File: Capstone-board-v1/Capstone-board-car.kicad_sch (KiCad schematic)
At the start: 25 parts, among them J1 Pcio Socket 1, J2 Pico Socket 2, J3 Ultra Sonic Sensor, J4 Car, J5 Camera, U1 3.3V Voltage Regulator, U2 555 Timer, U3 5V Voltage Regulator 2, U4 5V Voltage Regulator 1

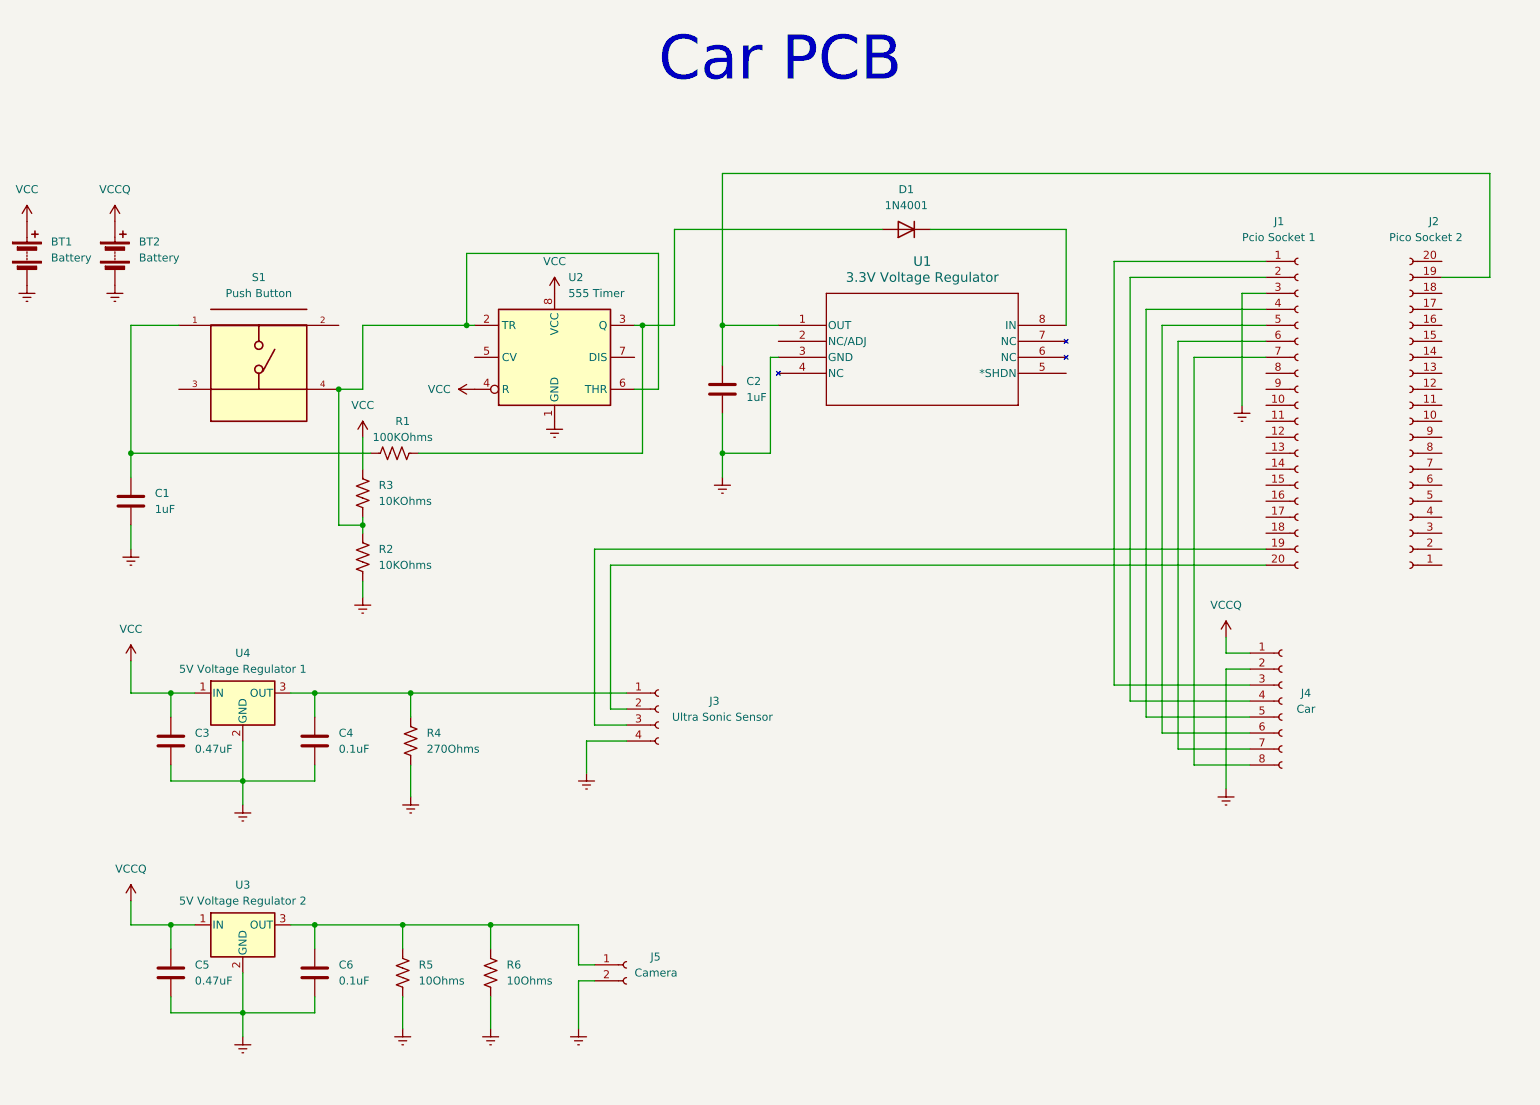
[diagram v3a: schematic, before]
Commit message: traces added
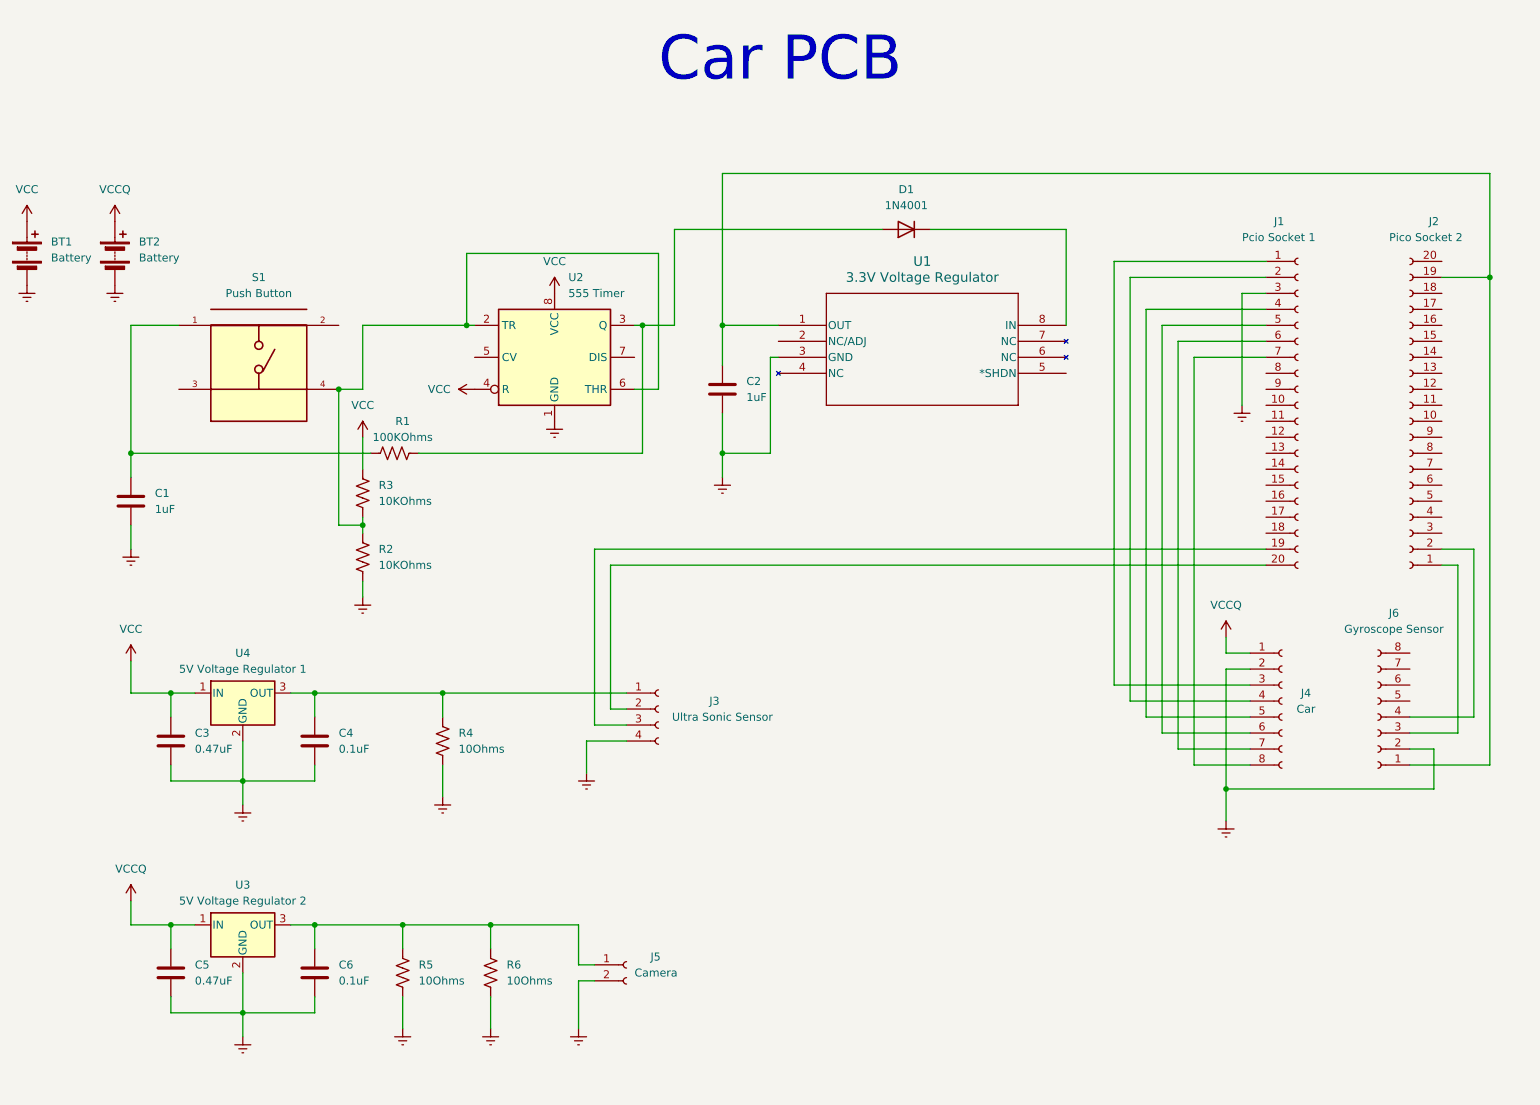
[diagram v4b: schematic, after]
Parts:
- added J6: Gyroscope Sensor, Connector_PinSocket_2.54mm:PinSocket_1x08_P2.54mm_Vertical, symbol Connector:Conn_01x08_Socket
- BT1: footprint Battery:Battery_Panasonic_CR1025-VSK_Vertical_CircularHoles -> Connector_Hirose:Hirose_DF11-4DP-2DSA_2x02_P2.00mm_Vertical
- BT2: footprint Battery:Battery_Panasonic_CR1025-VSK_Vertical_CircularHoles -> Connector_PinHeader_2.54mm:PinHeader_1x02_P2.54mm_Vertical
- R4: value 270Ohms -> 10Ohms
- S1: footprint TS02-66-60-BK-100-LCR-D:SW_TS02-66-60-BK-160-LCR-D -> TS:SW_TS02-66-60-BK-160-LCR-D
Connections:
- net Earth: now also J6.2 (Pin_2)
- net at C2.1, J2.19 (Pin_19), U1.1 (OUT): now also J6.1 (Pin_1)
- net at J2.1 (Pin_1): now also J6.3 (Pin_3)
- net at J2.2 (Pin_2): now also J6.4 (Pin_4)

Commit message: All routing done.
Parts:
- U3, U4: footprint LinReg:TO255P1040X460X1968-3 -> Connector_Hirose:Hirose_DF13-03P-1.25DSA_1x03_P1.25mm_Vertical
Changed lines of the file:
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@@
       (effects (font (size 1.27 1.27)))
     )
-    (property "Footprint" "LinReg:TO255P1040X460X1968-3" (at 71.755 165.1 0)
+    (property "Footprint" "Connector_Hirose:Hirose_DF13-03P-1.25DSA_1x03_P1.25mm_Vertical" (at 71.755 165.1 0)
       (effects (font (size 1.27 1.27) italic) (justify left) hide)
     )
@@
       (effects (font (size 1.27 1.27)))
     )
-    (property "Footprint" "LinReg:TO255P1040X460X1968-3" (at 71.755 128.27 0)
+    (property "Footprint" "Connector_Hirose:Hirose_DF13-03P-1.25DSA_1x03_P1.25mm_Vertical" (at 71.755 128.27 0)
       (effects (font (size 1.27 1.27) italic) (justify left) hide)
     )

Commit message: Some footprints fixed.
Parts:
- U3, U4: footprint Connector_Hirose:Hirose_DF13-03P-1.25DSA_1x03_P1.25mm_Vertical -> LinReg:TO255P1040X460X1968-3
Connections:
- net at J2.1 (Pin_1): now also J6.4 (Pin_4); no longer J6.3 (Pin_3)
- net at J2.2 (Pin_2): now also J6.3 (Pin_3); no longer J6.4 (Pin_4)
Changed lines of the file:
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@@
+    (stroke (width 0) (type default))
+  )
+  (wire (pts (xy 264.16 104.14) (xy 264.16 128.27))
     (stroke (width 0) (type default))
   )
@@
     (stroke (width 0) (type default))
   )
-  (wire (pts (xy 256.54 130.81) (xy 264.16 130.81))
-    (stroke (width 0) (type default))
-  )
-  (wire (pts (xy 264.16 130.81) (xy 264.16 104.14))
-    (stroke (width 0) (type default))
-  )
   (wire (pts (xy 78.74 161.29) (xy 82.55 161.29))
     (stroke (width 0) (type default))
@@
     (stroke (width 0) (type default))
   )
+  (wire (pts (xy 256.54 128.27) (xy 264.16 128.27))
+    (stroke (width 0) (type default))
+  )
   (wire (pts (xy 71.12 132.08) (xy 71.12 138.43))
     (stroke (width 0) (type default))
@@
     (stroke (width 0) (type default))
   )
+  (wire (pts (xy 266.7 101.6) (xy 266.7 130.81))
+    (stroke (width 0) (type default))
+  )
   (wire (pts (xy 264.16 104.14) (xy 261.62 104.14))
     (stroke (width 0) (type default))
@@
     (stroke (width 0) (type default))
   )
-  (wire (pts (xy 266.7 128.27) (xy 266.7 101.6))
-    (stroke (width 0) (type default))
-  )
   (wire (pts (xy 90.17 66.04) (xy 106.68 66.04))
     (stroke (width 0) (type default))
@@
     (stroke (width 0) (type default))
   )
-  (wire (pts (xy 256.54 128.27) (xy 266.7 128.27))
-    (stroke (width 0) (type default))
-  )
   (wire (pts (xy 129.54 127) (xy 129.54 104.14))
     (stroke (width 0) (type default))
@@
   )
   (wire (pts (xy 233.68 71.12) (xy 222.25 71.12))
+    (stroke (width 0) (type default))
+  )
+  (wire (pts (xy 256.54 130.81) (xy 266.7 130.81))
     (stroke (width 0) (type default))
   )
@@
       (effects (font (size 1.27 1.27)))
     )
-    (property "Footprint" "Connector_Hirose:Hirose_DF13-03P-1.25DSA_1x03_P1.25mm_Vertical" (at 71.755 165.1 0)
+    (property "Footprint" "LinReg:TO255P1040X460X1968-3" (at 71.755 165.1 0)
       (effects (font (size 1.27 1.27) italic) (justify left) hide)
     )
@@
       (effects (font (size 1.27 1.27)))
     )
-    (property "Footprint" "Connector_Hirose:Hirose_DF13-03P-1.25DSA_1x03_P1.25mm_Vertical" (at 71.755 128.27 0)
+    (property "Footprint" "LinReg:TO255P1040X460X1968-3" (at 71.755 128.27 0)
       (effects (font (size 1.27 1.27) italic) (justify left) hide)
     )

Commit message: Final traces done
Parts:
- U1, U2: footprint Package_DIP:DIP-8_W7.62mm -> Package_DIP:DIP-8_W7.62mm_Socket
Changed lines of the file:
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@@
-    )
-  )
-  (symbol (lib_id "Regulator_Linear:L7805") (at 71.12 161.29 0) (unit 1)
-    (in_bom yes) (on_board yes) (dnp no) (fields_autoplaced)
-    (property "Reference" "U3" (at 71.12 154.94 0)
-      (effects (font (size 1.27 1.27)))
-    )
-    (property "Value" "5V Voltage Regulator 2" (at 71.12 157.48 0)
-      (effects (font (size 1.27 1.27)))
-    )
-    (property "Footprint" "LinReg:TO255P1040X460X1968-3" (at 71.755 165.1 0)
-      (effects (font (size 1.27 1.27) italic) (justify left) hide)
-    )
-    (property "Datasheet" "http://www.st.com/content/ccc/resource/technical/document/datasheet/41/4f/b3/b0/12/d4/47/88/CD00000444.pdf/files/CD00000444.pdf/jcr:content/translations/en.CD00000444.pdf" (at 71.12 162.56 0)
-      (effects (font (size 1.27 1.27)) hide)
-    )
-    (pin "1")
-    (pin "2")
-    (pin "3")
-    (instances
-      (project "Capstone-board-car"
-        (path "/5a0b0107-0183-4094-a3d7-2a417dfae25a"
-          (reference "U3") (unit 1)
-        )
-      )
     )
   )
@@
       (effects (font (size 1.27 1.27)) (justify left))
     )
-    (property "Footprint" "Package_DIP:DIP-8_W7.62mm" (at 137.16 81.28 0)
+    (property "Footprint" "Package_DIP:DIP-8_W7.62mm_Socket" (at 137.16 81.28 0)
       (effects (font (size 1.27 1.27)) hide)
     )
@@
         (path "/5a0b0107-0183-4094-a3d7-2a417dfae25a"
           (reference "#PWR021") (unit 1)
+        )
+      )
+    )
+  )
+  (symbol (lib_id "Regulator_Linear:L7805") (at 71.12 161.29 0) (unit 1)
+    (in_bom yes) (on_board yes) (dnp no) (fields_autoplaced)
+    (property "Reference" "U3" (at 71.12 154.94 0)
+      (effects (font (size 1.27 1.27)))
+    )
+    (property "Value" "5V Voltage Regulator 2" (at 71.12 157.48 0)
+      (effects (font (size 1.27 1.27)))
+    )
+    (property "Footprint" "LinReg:TO255P1040X460X1968-3" (at 71.755 165.1 0)
+      (effects (font (size 1.27 1.27) italic) (justify left) hide)
+    )
+    (property "Datasheet" "http://www.st.com/content/ccc/resource/technical/document/datasheet/41/4f/b3/b0/12/d4/47/88/CD00000444.pdf/files/CD00000444.pdf/jcr:content/translations/en.CD00000444.pdf" (at 71.12 162.56 0)
+      (effects (font (size 1.27 1.27)) hide)
+    )
+    (pin "1")
+    (pin "2")
+    (pin "3")
+    (instances
+      (project "Capstone-board-car"
+        (path "/5a0b0107-0183-4094-a3d7-2a417dfae25a"
+          (reference "U3") (unit 1)
         )
       )
@@
       (effects (font (size 1.524 1.524)))
     )
-    (property "Footprint" "Package_DIP:DIP-8_W7.62mm" (at 156.21 66.04 0)
+    (property "Footprint" "Package_DIP:DIP-8_W7.62mm_Socket" (at 156.21 66.04 0)
       (effects (font (size 1.27 1.27) italic) hide)
     )

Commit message: Final PCB completed!
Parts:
- removed D1: 1N4001, Diode_THT:D_DO-41_SOD81_P10.16mm_Horizontal, symbol Diode:1N4001
- J1: value Pcio Socket 1 -> Pico Socket 1
- U1: value 3.3V Voltage Regulator -> 3.3V V.R
- U3: value 5V Voltage Regulator 2 -> 5V V.R 2
- U4: value 5V Voltage Regulator 1 -> 5V V.R 1
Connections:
- net at R1.2, U2.3 (Q): now also U1.8 (IN)
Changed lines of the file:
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@@
-    (stroke (width 0) (type default))
-  )
-  (wire (pts (xy 139.7 50.8) (xy 172.72 50.8))
     (stroke (width 0) (type default))
   )
@@
     (stroke (width 0) (type default))
   )
-  (wire (pts (xy 180.34 50.8) (xy 201.93 50.8))
+  (wire (pts (xy 139.7 50.8) (xy 201.93 50.8))
     (stroke (width 0) (type default))
   )
@@
       (effects (font (size 1.27 1.27)))
     )
-    (property "Value" "5V Voltage Regulator 2" (at 71.12 157.48 0)
+    (property "Value" "5V V.R 2" (at 71.12 157.48 0)
       (effects (font (size 1.27 1.27)))
     )
@@
         (path "/5a0b0107-0183-4094-a3d7-2a417dfae25a"
           (reference "U3") (unit 1)
-        )
-      )
-    )
-  )
-  (symbol (lib_id "Diode:1N4001") (at 176.53 50.8 180) (unit 1)
-    (in_bom yes) (on_board yes) (dnp no) (fields_autoplaced)
-    (property "Reference" "D1" (at 176.53 44.45 0)
-      (effects (font (size 1.27 1.27)))
-    )
-    (property "Value" "1N4001" (at 176.53 46.99 0)
-      (effects (font (size 1.27 1.27)))
-    )
-    (property "Footprint" "Diode_THT:D_DO-41_SOD81_P10.16mm_Horizontal" (at 176.53 50.8 0)
-      (effects (font (size 1.27 1.27)) hide)
-    )
-    (property "Datasheet" "http://www.vishay.com/docs/88503/1n4001.pdf" (at 176.53 50.8 0)
-      (effects (font (size 1.27 1.27)) hide)
-    )
-    (property "Sim.Device" "D" (at 176.53 50.8 0)
-      (effects (font (size 1.27 1.27)) hide)
-    )
-    (property "Sim.Pins" "1=K 2=A" (at 176.53 50.8 0)
-      (effects (font (size 1.27 1.27)) hide)
-    )
-    (pin "1")
-    (pin "2")
-    (instances
-      (project "Capstone-board-car"
-        (path "/5a0b0107-0183-4094-a3d7-2a417dfae25a"
-          (reference "D1") (unit 1)
         )
       )
@@
       (effects (font (size 1.27 1.27)) (justify left))
     )
-    (property "Value" "Pcio Socket 1" (at 229.87 52.07 0)
+    (property "Value" "Pico Socket 1" (at 229.87 52.07 0)
       (effects (font (size 1.27 1.27)) (justify left))
     )
@@
       (effects (font (size 1.524 1.524)))
     )
-    (property "Value" "3.3V Voltage Regulator" (at 179.07 58.42 0)
+    (property "Value" "3.3V V.R" (at 179.07 58.42 0)
       (effects (font (size 1.524 1.524)))
     )
@@
       (effects (font (size 1.27 1.27)))
     )
-    (property "Value" "5V Voltage Regulator 1" (at 71.12 120.65 0)
-      (effects (font (size 1.27 1.27)))
-    )
+    (property "Value" "5V V.R 1" (at 71.12 120.65 0)
+      (effects (font (size 1.27 1.27)))
+    )
